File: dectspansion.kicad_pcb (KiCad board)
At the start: 4 copper layers, 37 x 36.6 mm, 24 parts, among them J1 Hexpansion-Connector, J2 Conn_01x03_Pin, J3 AudioJack4, J4 Conn_01x02_Pin, U1 SC14CVMDECT

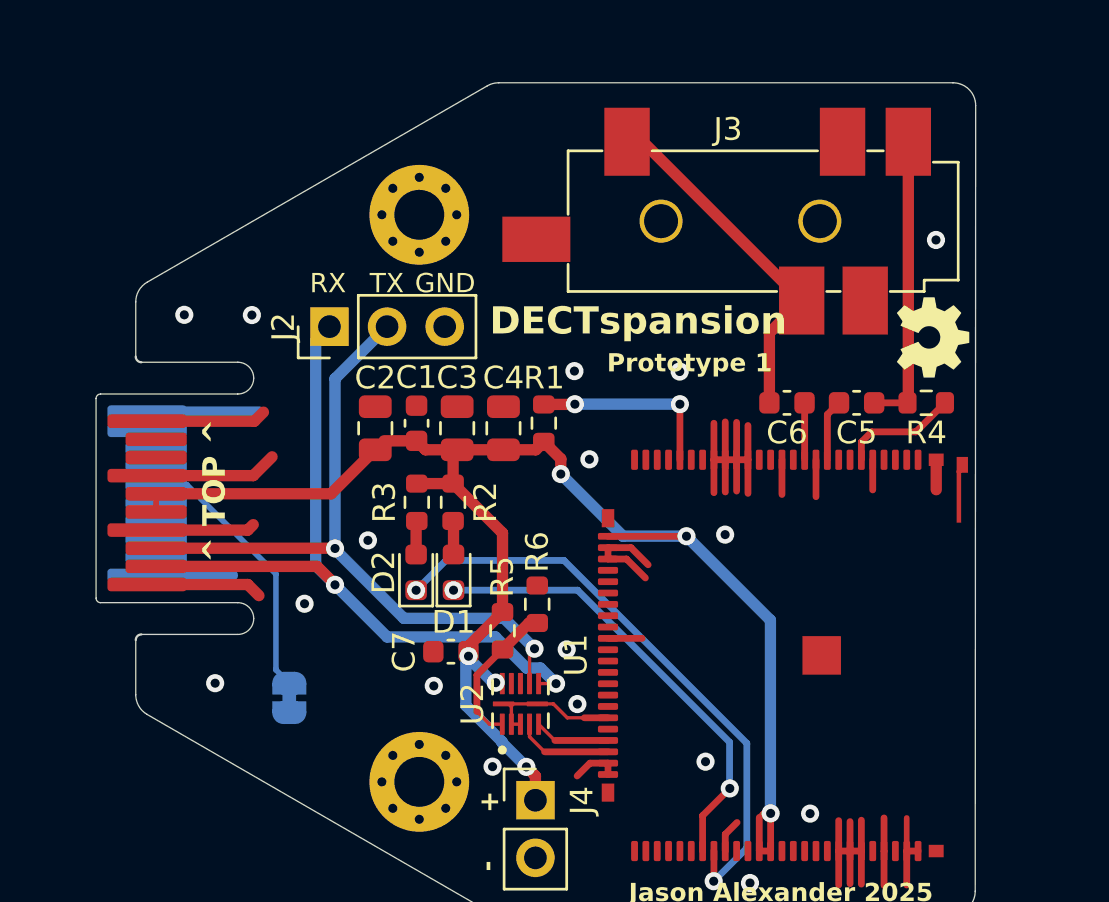
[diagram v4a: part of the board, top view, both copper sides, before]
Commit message: Added eeprom to board, updated to prototype 2
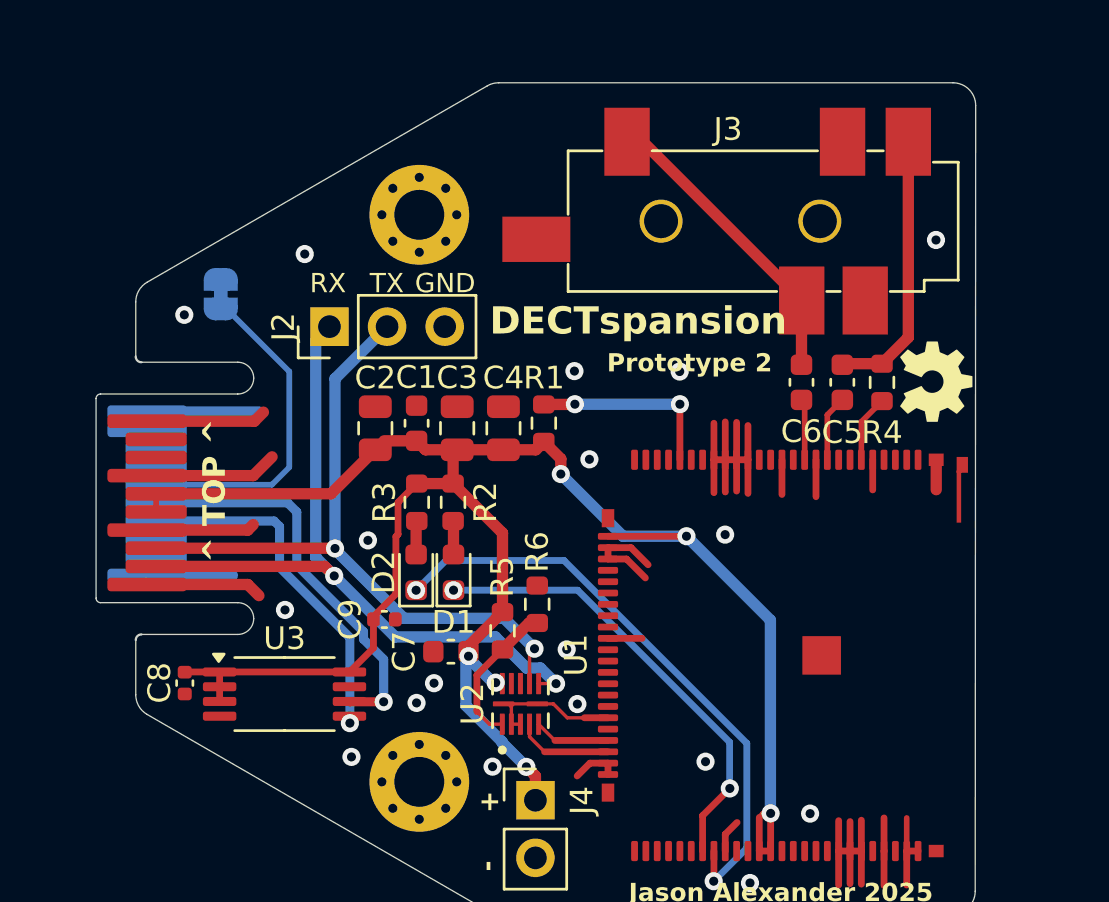
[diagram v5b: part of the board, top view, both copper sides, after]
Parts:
- added C8: 1u, Capacitor_SMD:C_0402_1005Metric, F.Cu at (102.2, 108.1)
- added C9: 1u, Capacitor_SMD:C_0402_1005Metric, F.Cu at (111.0, 105.3)
- added U3: 24LC00, Package_SO:TSSOP-8_4.4x3mm_P0.65mm, F.Cu at (106.6, 108.6)
- moved JP1 18.1 mm to (103.8, 91.0), turned to 90 degrees
- moved R4 2.15 mm to (132.9, 94.9), turned to -90 degrees
- moved C6 1.11 mm to (129.3, 94.9), turned to -90 degrees
- moved C5 1.10 mm to (131.2, 94.9), turned to 90 degrees
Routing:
- net +3V3: track 71.0 -> 89.1 mm
- net /SCL: track 0.00 -> 17.8 mm, vias 0 -> 1
- net /SDA: track 0.00 -> 15.8 mm, vias 0 -> 1
- net /HEXP_DET: track 12.0 -> 14.6 mm
- net /Left: track 15.7 -> 13.4 mm
- net Net-(U1-VREFp): track 5.22 -> 2.96 mm
- net /Mic: track 12.7 -> 12.0 mm
- net GND: vias 17 -> 18
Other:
- board text added: "Prototype 2"

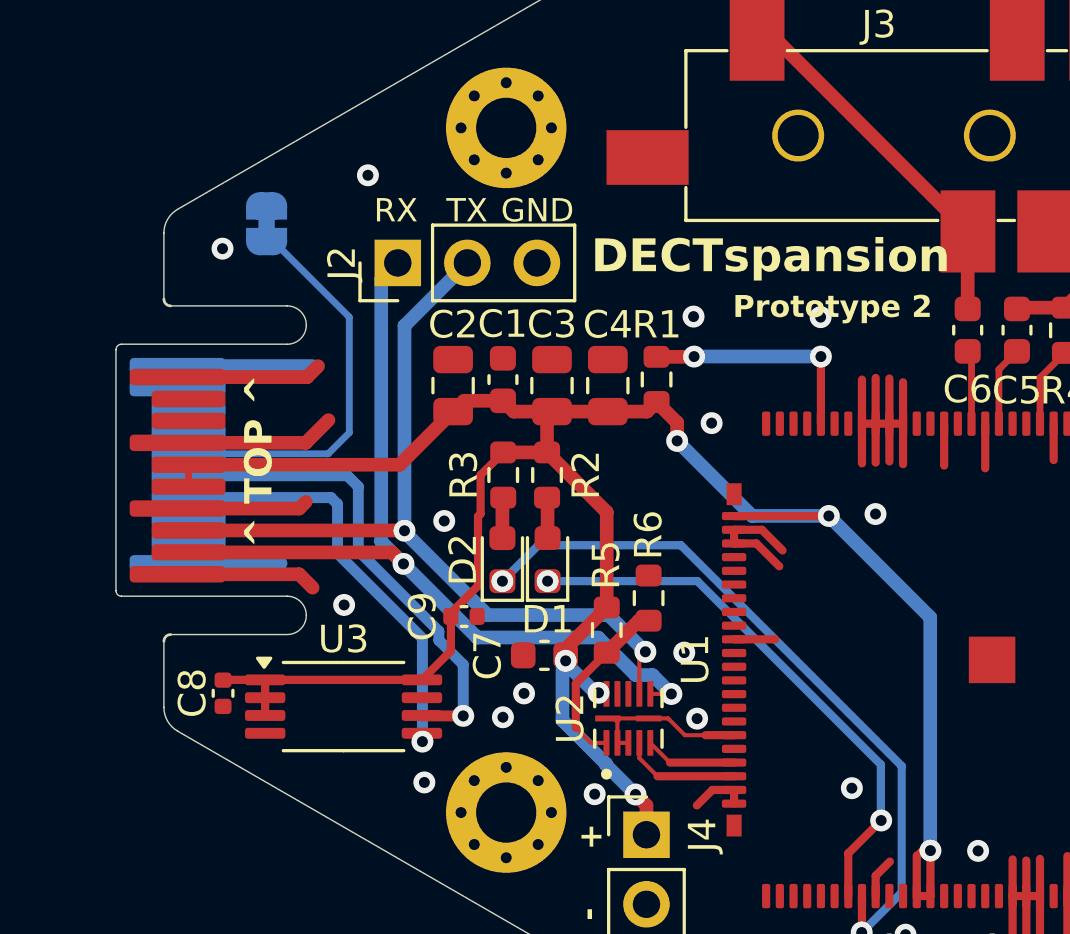
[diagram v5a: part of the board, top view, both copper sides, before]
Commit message: Removed eeprom capacitors, and solder jumper
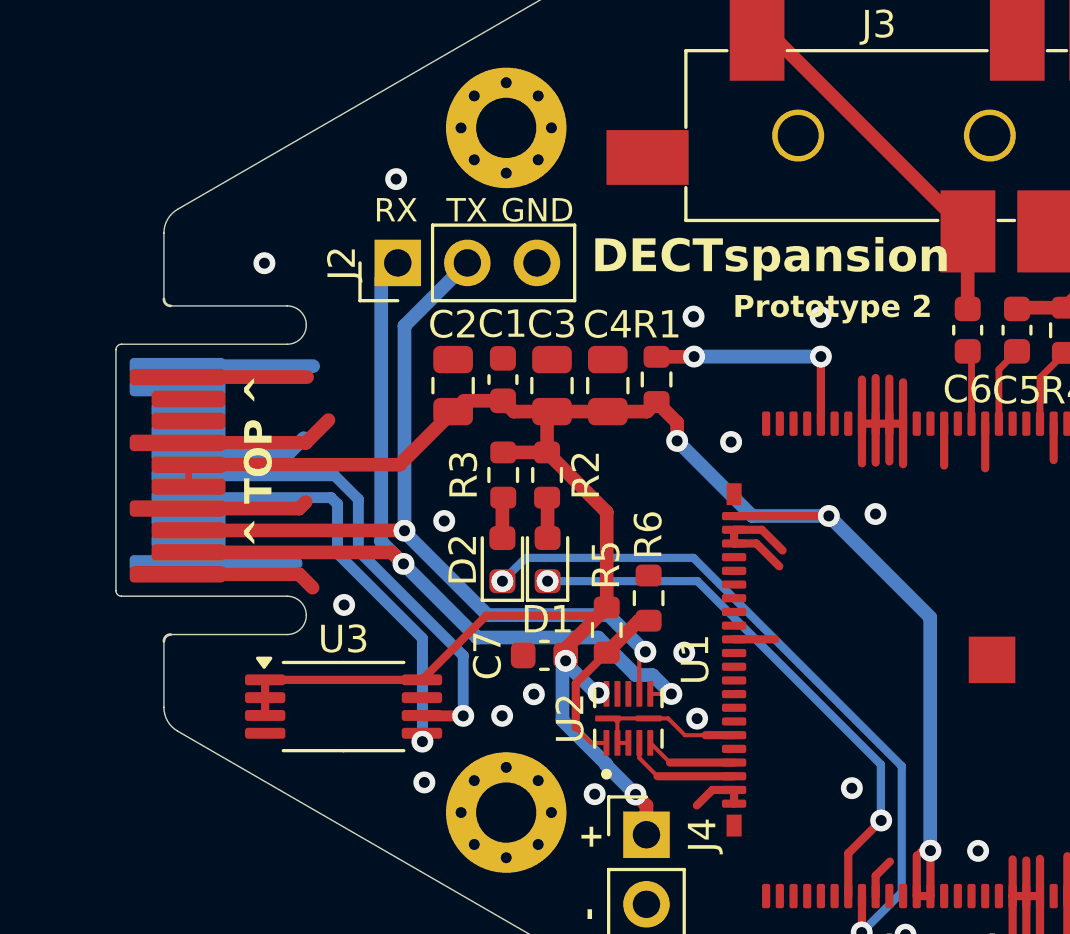
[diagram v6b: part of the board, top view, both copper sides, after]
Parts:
- removed C8, C9: 1u, Capacitor_SMD:C_0402_1005Metric
- removed JP1: SolderJumper_2_Bridged, Jumper:SolderJumper-2_P1.3mm_Bridged_RoundedPad1.0x1.5mm
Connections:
- J1 pad 6: /HEXP_DET -> GND
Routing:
- net /HEXP_DET: track 14.6 -> 0.00 mm
- net GND: track 81.1 -> 85.6 mm
- net +3V3: track 89.1 -> 85.9 mm

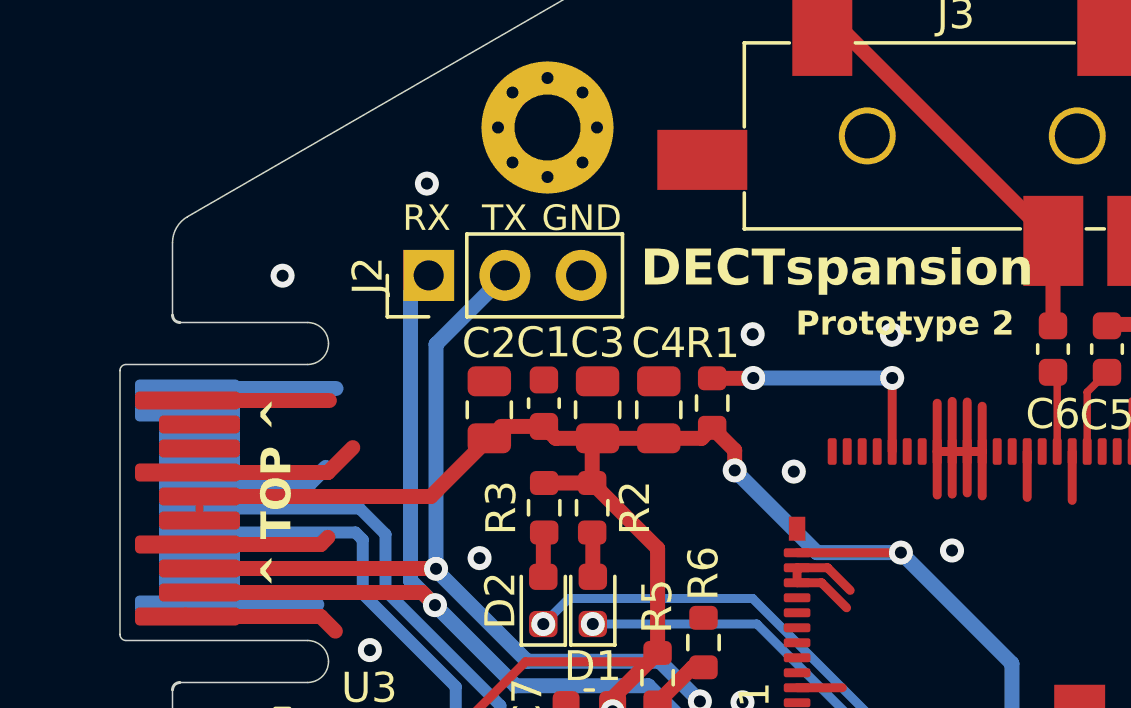
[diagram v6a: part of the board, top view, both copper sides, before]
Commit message: Added piezo ringer
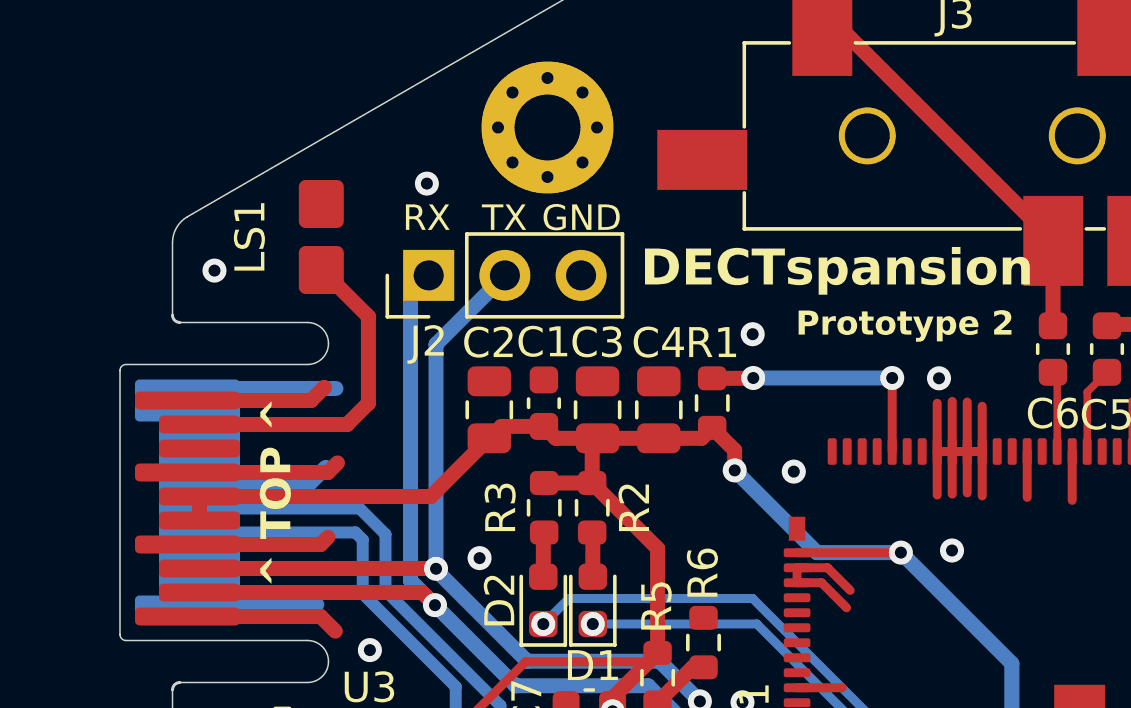
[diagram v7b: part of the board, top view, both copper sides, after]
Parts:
- added LS1: ~, micro_piezo:CMT-322-65-SMT-TR, F.Cu at (105.0, 91.2)
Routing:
- net /HS_F: track 0.00 -> 11.0 mm
- net GND: track 85.6 -> 84.9 mm
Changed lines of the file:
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@@
 		(embedded_fonts no)
 	)
+	(footprint "micro_piezo:CMT-322-65-SMT-TR"
+		(layer "F.Cu")
+		(at 104.96 91.15 180)
+		(property "Reference" "LS1"
+			(at 2.36 0 90)
+			(unlocked yes)
+			(layer "F.SilkS")
+			(effects
+				(font
+					(size 1 1)
+					(thickness 0.1)
+				)
+			)
+		)
+		(property "Value" "~"
+			(at 0 2.75 180)
+			(unlocked yes)
+			(layer "F.Fab")
+			(hide yes)
+			(effects
+				(font
+					(size 1 1)
+					(thickness 0.15)
+				)
+			)
+		)
+		(property "Datasheet" ""
+			(at 0 0 180)
+			(unlocked yes)
+			(layer "F.Fab")
+			(hide yes)
+			(effects
+				(font
+					(size 1 1)
+					(thickness 0.15)
+				)
+			)
+		)
+		(property "Description" ""
+			(at 0 0 180)
+			(unlocked yes)
+			(layer "F.Fab")
+			(hide yes)
+			(effects
+				(font
+					(size 1 1)
+					(thickness 0.15)
+				)
+			)
+		)
+		(sheetname "/")
+		(sheetfile "dectspansion.kicad_sch")
+		(attr smd)
+		(fp_rect
+			(start -1.8 -2)
+			(end 1.8 2)
+			(stroke
+				(width 0.05)
+				(type solid)
+			)
+			(fill no)
+			(layer "F.CrtYd")
+		)
+		(fp_rect
+			(start -1.6 -1.6)
+			(end 1.6 1.6)
+			(stroke
+				(width 0.1)
+				(type solid)
+			)
+			(fill no)
+			(layer "F.Fab")
+		)
+		(pad "1" smd roundrect
+			(at 0 -1.1 180)
+			(size 1.5 1.6)
+			(layers "F.Cu" "F.Mask" "F.Paste")
+			(roundrect_rratio 0.15)
+			(net 8 "/HS_F")
+			(pintype "passive")
+			(thermal_bridge_angle 45)
+		)
+		(pad "2" smd roundrect
+			(at 0 1.1 180)
+			(size 1.5 1.6)
+			(layers "F.Cu" "F.Mask" "F.Paste")
+			(roundrect_rratio 0.15)
+			(net 2 "GND")
+			(pintype "passive")
+			(thermal_bridge_angle 45)
+		)
+		(embedded_fonts no)
+	)
 	(footprint "Resistor_SMD:R_0603_1608Metric"
 		(layer "F.Cu")
@@
 		(tags "Through hole pin header THT 1x03 2.54mm single row")
 		(property "Reference" "J2"
-			(at -0.01 -2.03 270)
+			(at -2.21 0 180)
 			(layer "F.SilkS")
 			(effects
@@
 		(start 100.9 99.8)
 		(end 100.9 100.6)
-		(width 0.25)
+		(width 0.5)
 		(layer "F.Cu")
 		(net 1)
@@
 	)
 	(segment
-		(start 105.18 99)
-		(end 106.01 98.17)
-		(width 0.5)
-		(layer "F.Cu")
-		(net 2)
-	)
-	(segment
 		(start 104.94 101.4)
 		(end 105.18 101.16)
@@
 	)
 	(segment
-		(start 100.5 99)
-		(end 105.18 99)
-		(width 0.5)
-		(layer "F.Cu")
-		(net 2)
-	)
-	(segment
 		(start 120.82 109.675)
 		(end 119.775 109.675)
@@
 	)
 	(segment
+		(start 100.5 96.6)
+		(end 104.62 96.6)
+		(width 0.5)
+		(layer "F.Cu")
+		(net 2)
+	)
+	(segment
 		(start 125.49 98.3)
 		(end 125.49 99.75)
@@
 	)
 	(segment
+		(start 104.62 96.6)
+		(end 105.05 96.17)
+		(width 0.5)
+		(layer "F.Cu")
+		(net 2)
+	)
+	(segment
 		(start 116.56 109.1875)
 		(end 116.56 109.9575)
@@
 	)
 	(segment
+		(start 105.18 99)
+		(end 105.5 98.68)
+		(width 0.5)
+		(layer "F.Cu")
+		(net 2)
+	)
+	(segment
 		(start 120.82 102.175)
 		(end 121.835 102.175)
@@
 	)
 	(segment
+		(start 100.5 99)
+		(end 105.18 99)
+		(width 0.5)
+		(layer "F.Cu")
+		(net 2)
+	)
+	(segment
 		(start 125.99 114.81)
 		(end 126.51 114.29)
@@
 	)
 	(segment
-		(start 100.5 96.6)
-		(end 105.23 96.6)
-		(width 0.5)
-		(layer "F.Cu")
-		(net 2)
-	)
-	(segment
 		(start 125.49 98.3)
 		(end 125.49 96.69)
@@
 	)
 	(segment
+		(start 105.05 96.17)
+		(end 105.07 96.17)
+		(width 0.5)
+		(layer "F.Cu")
+		(net 2)
+	)
+	(segment
 		(start 129.99 98.3)
 		(end 129.99 99.93)
@@
 	)
 	(via
-		(at 103.67 92.44)
+		(at 101.4 92.27)
 		(size 0.8)
 		(drill 0.4)
@@
 	)
 	(via
-		(at 123.98 94.41)
+		(at 125.55 95.86)
 		(size 0.8)
 		(drill 0.4)
@@
 	)
 	(segment
+		(start 105.82 97.4)
+		(end 106.53 96.69)
+		(width 0.5)
+		(layer "F.Cu")
+		(net 8)
+	)
+	(segment
+		(start 106.53 96.69)
+		(end 106.53 93.8)
+		(width 0.5)
+		(layer "F.Cu")
+		(net 8)
+	)
+	(segment
+		(start 100.9 97.4)
+		(end 105.82 97.4)
+		(width 0.5)
+		(layer "F.Cu")
+		(net 8)
+	)
+	(segment
+		(start 106.53 93.8)
+		(end 104.98 92.25)
+		(width 0.5)
+		(layer "F.Cu")
+		(net 8)
+	)
+	(segment
+		(start 104.98 92.25)
+		(end 104.96 92.25)
+		(width 0.5)
+		(layer "F.Cu")
+		(net 8)
+	)
+	(segment
